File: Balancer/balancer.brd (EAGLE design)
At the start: 145 x 220 mm, 285 parts, among them Q1 BSS123W, Q10A SIR882DP-T1-GE3, Q10B SIS468DN-T1-GE3, Q11A SIR882DP-T1-GE3, Q11B SIS468DN-T1-GE3, Q12A SIR882DP-T1-GE3, Q12B SIS468DN-T1-GE3, Q2 BSS123W, Q3A SIR882DP-T1-GE3, Q3B SIS468DN-T1-GE3, Q4 MMBT3906LT1G, Q4A SIR882DP-T1-GE3, Q4B SIS468DN-T1-GE3, Q5 FDN5618P, Q5A SIR882DP-T1-GE3, Q5B SIS468DN-T1-GE3, Q6 CMPT3904E_TR_PBFREE, Q6A SIR882DP-T1-GE3, Q6B SIS468DN-T1-GE3, Q9A SIR882DP-T1-GE3, Q9B SIS468DN-T1-GE3, T10 750312504, T11 750312504, T12 750312504, T3 750312504, T4 750312504, T5 750312504, T6 750312504, T9 750312504, U1 LTC3300ILXE-1PBF, U2 LTC3300ILXE-1PBF

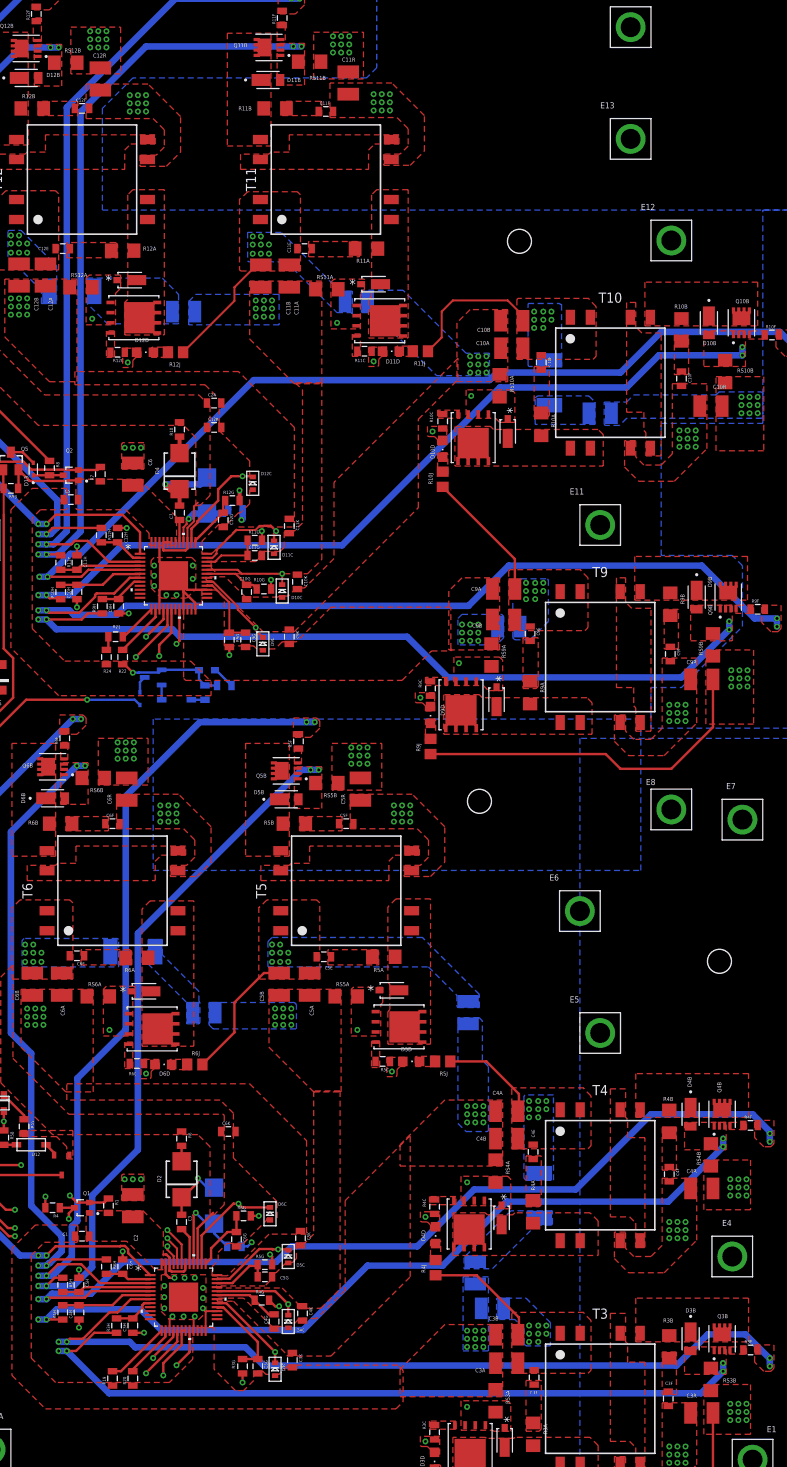
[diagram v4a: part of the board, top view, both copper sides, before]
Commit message: replaced RSnA and RSnB to correct parts
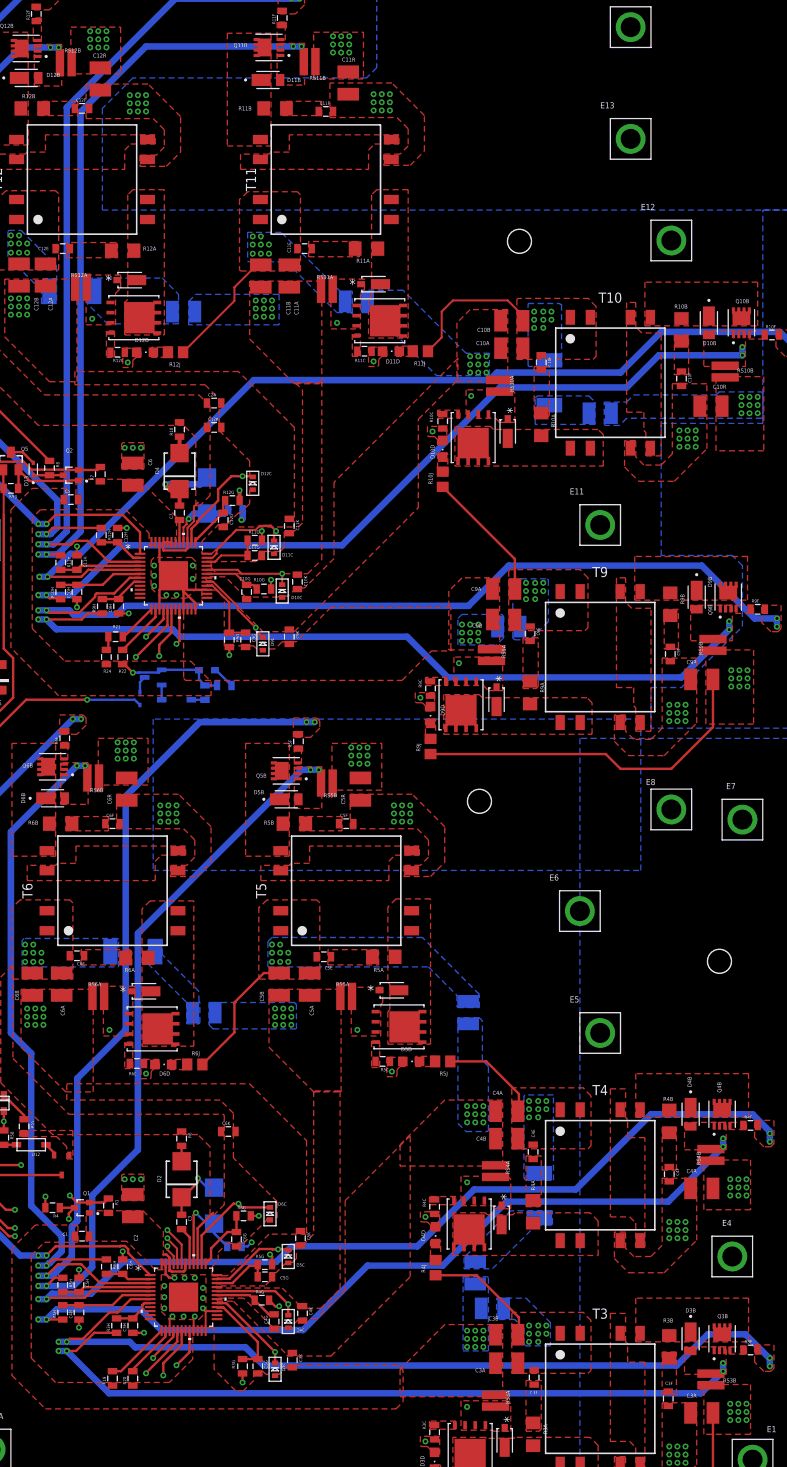
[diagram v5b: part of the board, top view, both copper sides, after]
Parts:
- RS10A, RS10B, RS11A, RS11B, RS12A, RS12B, RS3A, RS3B, RS4A, RS4B, RS5A, RS5B, RS6A, RS6B, RS9A, RS9B: device rcl:R1206 -> PRL1632-R010-F-T1:RESC1632X60N

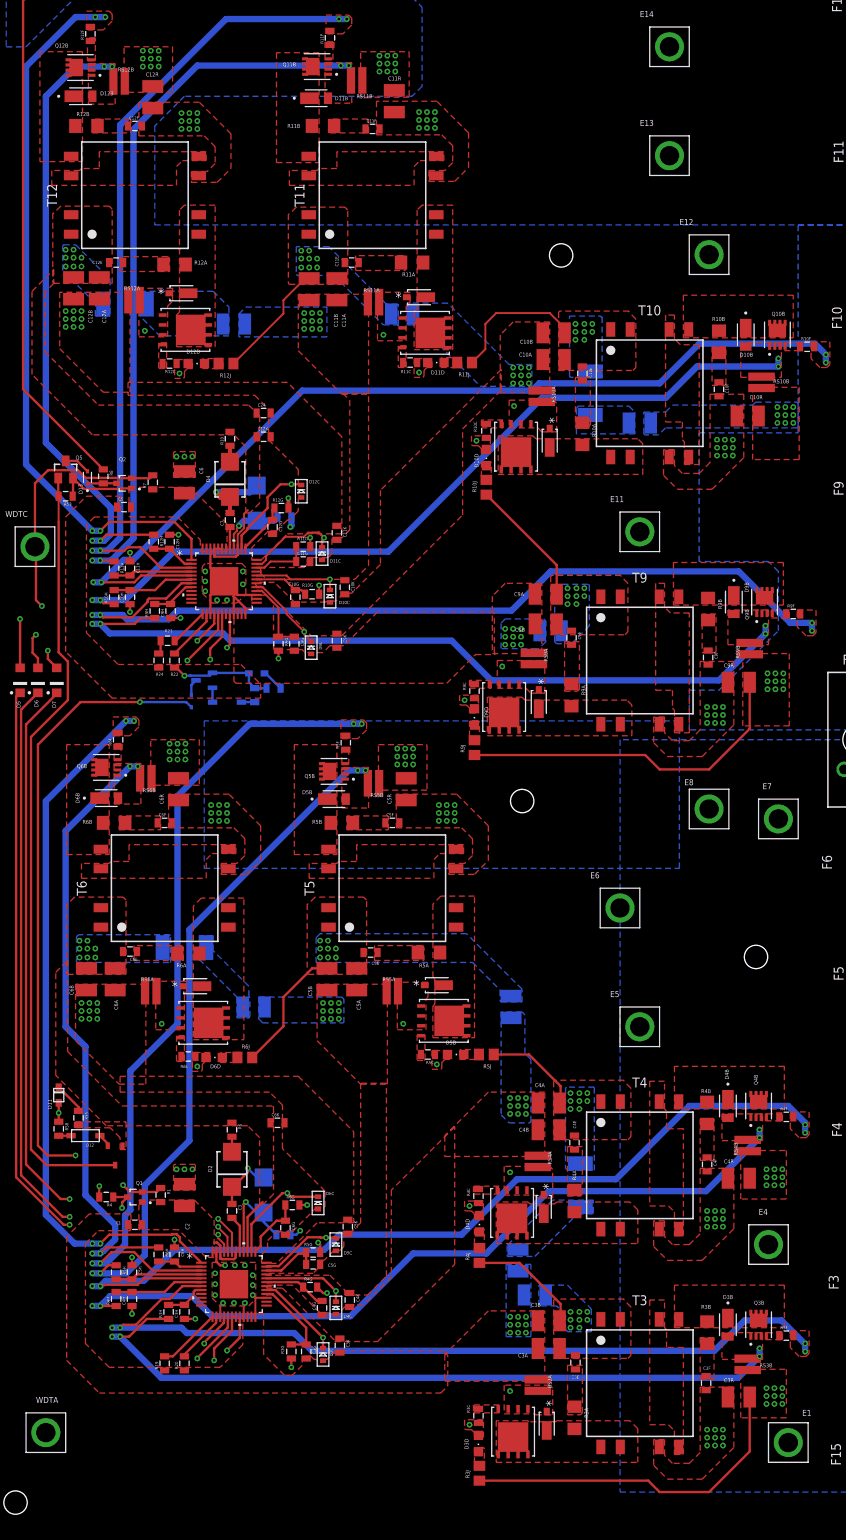
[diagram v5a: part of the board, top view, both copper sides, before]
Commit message: placed RSnA and RSnB
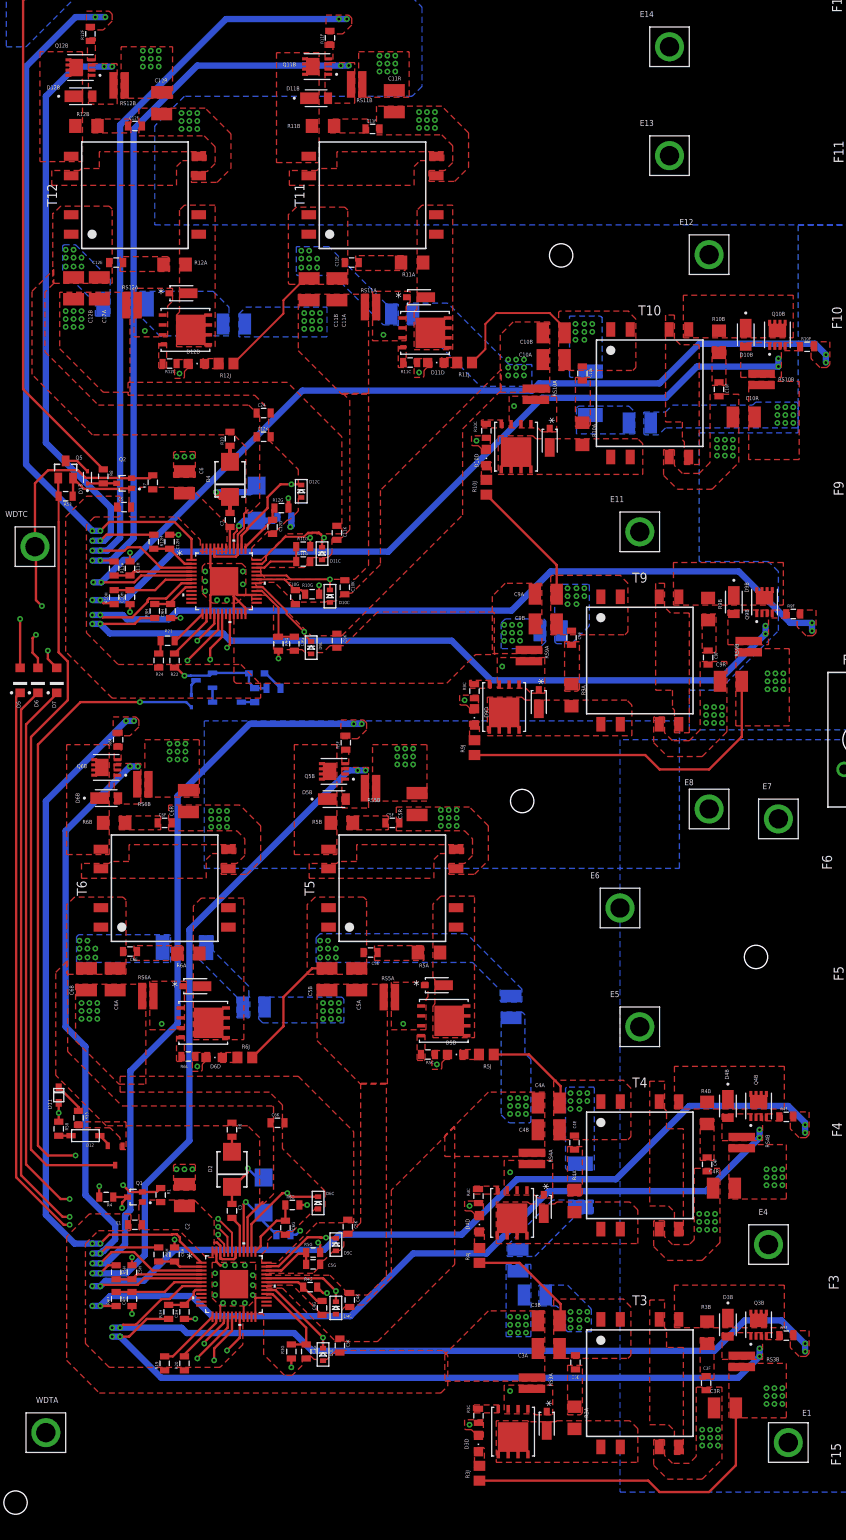
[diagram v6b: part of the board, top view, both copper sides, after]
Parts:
- moved C5R 2.36 mm to (56.5, 94.6)
- moved C4R 2.29 mm to (95.9, 45.3)
- moved C3R 2.26 mm to (96.0, 17.1)
- moved C6R 1.98 mm to (27.2, 95.0)
- moved C12R 1.37 mm to (23.7, 184.5)
- moved C9R 1.02 mm to (96.8, 110.4)
- moved RS3B 0.85 mm to (98.2, 23.1)
- moved RS4A 0.85 mm to (71.2, 49.1)
- moved RS4B 0.85 mm to (98.2, 51.2)
- moved RS5A 0.85 mm to (53.0, 69.8)
- moved RS6B 0.85 mm to (21.3, 97.2)
- moved RS10A 0.80 mm to (71.8, 147.2)
- moved RS3A 0.80 mm to (71.2, 20.3)
- moved RS9A 0.74 mm to (70.9, 113.7)
- moved RS11A 0.74 mm to (50.5, 158.4)
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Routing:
- net V-: track 105.3 -> 103.2 mm
- net BOT6_TS: track 99.1 -> 99.8 mm
